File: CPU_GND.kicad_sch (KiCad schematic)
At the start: 1 part

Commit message: Added LGA1151 socket bracket holes
stolen from another lga1151 footprint that has wrong pin numbers....
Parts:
- JCPU1: footprint A-my-stuff:LGA-1151_L47.1-W42.5-P0.91_PE115127-4041-01H -> A-my-stuff:LGA1151_TE-2287402-1
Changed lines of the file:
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@@
 			)
 		)
-		(property "Footprint" "A-my-stuff:LGA-1151_L47.1-W42.5-P0.91_PE115127-4041-01H"
+		(property "Footprint" "A-my-stuff:LGA1151_TE-2287402-1"
 			(at 203.2 256.54 0)
 			(effects
@@
 			)
 		)
-		(property "Footprint" "A-my-stuff:LGA-1151_L47.1-W42.5-P0.91_PE115127-4041-01H"
+		(property "Footprint" "A-my-stuff:LGA1151_TE-2287402-1"
 			(at 76.2 256.54 0)
 			(effects
@@
 			)
 		)
-		(property "Footprint" "A-my-stuff:LGA-1151_L47.1-W42.5-P0.91_PE115127-4041-01H"
+		(property "Footprint" "A-my-stuff:LGA1151_TE-2287402-1"
 			(at 139.7 256.54 0)
 			(effects

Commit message: Added CPU CFG resistors
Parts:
- JCPU1: footprint A-my-stuff:LGA1151_TE-2287402-1 -> A-my-stuff:LGA-1151_L47.1-W42.5-P0.91_PE115127-4041-01H
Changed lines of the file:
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@@
 			)
 		)
-		(property "Footprint" "A-my-stuff:LGA1151_TE-2287402-1"
+		(property "Footprint" "A-my-stuff:LGA-1151_L47.1-W42.5-P0.91_PE115127-4041-01H"
 			(at 203.2 256.54 0)
 			(effects
@@
 			)
 		)
-		(property "Footprint" "A-my-stuff:LGA1151_TE-2287402-1"
+		(property "Footprint" "A-my-stuff:LGA-1151_L47.1-W42.5-P0.91_PE115127-4041-01H"
 			(at 76.2 256.54 0)
 			(effects
@@
 			)
 		)
-		(property "Footprint" "A-my-stuff:LGA1151_TE-2287402-1"
+		(property "Footprint" "A-my-stuff:LGA-1151_L47.1-W42.5-P0.91_PE115127-4041-01H"
 			(at 139.7 256.54 0)
 			(effects

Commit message: stroopwafel.exe
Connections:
- net GND: no longer JCPU1.A11 (VSS), JCPU1.A13 (VSS), JCPU1.A15 (VSS), JCPU1.A17 (VSS), JCPU1.A24 (VSS), JCPU1.A4 (VSS), JCPU1.A7 (VSS), JCPU1.AA3 (VSS), JCPU1.AA33 (VSS), JCPU1.AA8 (VSS), JCPU1.AB39 (VSS), JCPU1.AB5 (VSS), JCPU1.AC3 (VSS), JCPU1.AC33 (VSS), JCPU1.AC34 (VSS), JCPU1.AC35 (VSS), JCPU1.AC6 (VSS), JCPU1.AD1 (VSS), JCPU1.AD33 (VSS), JCPU1.AD36 (VSS), JCPU1.AD37 (VSS), JCPU1.AD38 (VSS), JCPU1.AD39 (VSS), JCPU1.AD4 (VSS), JCPU1.AD40 (VSS), JCPU1.AD6 (VSS), JCPU1.AD7 (VSS), JCPU1.AD8 (VSS), JCPU1.AE3 (VSS), JCPU1.AE33 (VSS), JCPU1.AE36 (VSS), JCPU1.AE5 (VSS), JCPU1.AE8 (VSS), JCPU1.AF1 (VSS), JCPU1.AF33 (VSS), JCPU1.AF36 (VSS), JCPU1.AF37 (VSS), JCPU1.AF40 (VSS), JCPU1.AF5 (VSS), JCPU1.AF8 (VSS), JCPU1.AG1 (VSS), JCPU1.AG2 (VSS), JCPU1.AG3 (VSS), JCPU1.AG33 (VSS), JCPU1.AG36 (VSS), JCPU1.AG4 (VSS), JCPU1.AG5 (VSS), JCPU1.AG8 (VSS), JCPU1.AH33 (VSS), JCPU1.AH36 (VSS), JCPU1.AH37 (VSS), JCPU1.AH38 (VSS), JCPU1.AH39 (VSS), JCPU1.AH40 (VSS), JCPU1.AH5 (VSS), JCPU1.AH8 (VSS), JCPU1.AJ1 (VSS), JCPU1.AJ24 (VSS), JCPU1.AJ30 (VSS), JCPU1.AJ31 (VSS), JCPU1.AJ32 (VSS), JCPU1.AJ33 (VSS), JCPU1.AJ34 (VSS), JCPU1.AJ35 (VSS), JCPU1.AJ36 (VSS), JCPU1.AJ4 (VSS), JCPU1.AJ5 (VSS), JCPU1.AJ8 (VSS), JCPU1.AK10 (VSS), JCPU1.AK12 (VSS), JCPU1.AK13 (VSS), JCPU1.AK15 (VSS), JCPU1.AK16 (VSS), JCPU1.AK17 (VSS), JCPU1.AK18 (VSS), JCPU1.AK19 (VSS), JCPU1.AK20 (VSS), JCPU1.AK22 (VSS), JCPU1.AK23 (VSS), JCPU1.AK25 (VSS), JCPU1.AK26 (VSS), JCPU1.AK27 (VSS), JCPU1.AK28 (VSS), JCPU1.AK29 (VSS), JCPU1.AK30 (VSS), JCPU1.AK36 (VSS), JCPU1.AK37 (VSS), JCPU1.AK40 (VSS), JCPU1.AK5 (VSS), JCPU1.AK6 (VSS), JCPU1.AK7 (VSS), JCPU1.AK8 (VSS), JCPU1.AK9 (VSS), JCPU1.AL1 (VSS), JCPU1.AL11 (VSS), JCPU1.AL14 (VSS), JCPU1.AL2 (VSS), JCPU1.AL21 (VSS), JCPU1.AL24 (VSS), JCPU1.AL27 (VSS), JCPU1.AL3 (VSS), JCPU1.AL30 (VSS), JCPU1.AL36 (VSS), JCPU1.AL4 (VSS), JCPU1.AL5 (VSS), JCPU1.AM11 (VSS), JCPU1.AM14 (VSS), JCPU1.AM17 (VSS), JCPU1.AM19 (VSS), JCPU1.AM24 (VSS), JCPU1.AM27 (VSS), JCPU1.AM30 (VSS), JCPU1.AM31 (VSS), JCPU1.AM32 (VSS), JCPU1.AM33 (VSS), JCPU1.AM34 (VSS), JCPU1.AM35 (VSS), JCPU1.AM36 (VSS), JCPU1.AM37 (VSS), JCPU1.AM38 (VSS), JCPU1.AM39 (VSS), JCPU1.AM40 (VSS), JCPU1.AM5 (VSS), JCPU1.AN1 (VSS), JCPU1.AN10 (VSS), JCPU1.AN11 (VSS), JCPU1.AN14 (VSS), JCPU1.AN16 (VSS), JCPU1.AN19 (VSS), JCPU1.AN22 (VSS), JCPU1.AN23 (VSS), JCPU1.AN24 (VSS), JCPU1.AN27 (VSS), JCPU1.AN30 (VSS), JCPU1.AN36 (VSS), JCPU1.AN4 (VSS), JCPU1.AN5 (VSS), JCPU1.AN6 (VSS), JCPU1.AN7 (VSS), JCPU1.AN8 (VSS), JCPU1.AN9 (VSS), JCPU1.AP11 (VSS), JCPU1.AP14 (VSS), JCPU1.AP24 (VSS), JCPU1.AP27 (VSS), JCPU1.AP30 (VSS), JCPU1.AP36 (VSS), JCPU1.AP37 (VSS), JCPU1.AP40 (VSS), JCPU1.AP5 (VSS), JCPU1.AR1 (VSS), JCPU1.AR11 (VSS), JCPU1.AR14 (VSS), JCPU1.AR16 (VSS), JCPU1.AR17 (VSS), JCPU1.AR18 (VSS), JCPU1.AR19 (VSS), JCPU1.AR2 (VSS), JCPU1.AR20 (VSS), JCPU1.AR21 (VSS), JCPU1.AR22 (VSS), JCPU1.AR23 (VSS), JCPU1.AR24 (VSS), JCPU1.AR27 (VSS), JCPU1.AR3 (VSS), JCPU1.AR30 (VSS), JCPU1.AR31 (VSS), JCPU1.AR32 (VSS), JCPU1.AR33 (VSS), JCPU1.AR34 (VSS), JCPU1.AR35 (VSS), JCPU1.AR36 (VSS), JCPU1.AR4 (VSS), JCPU1.AR5 (VSS), JCPU1.AT10 (VSS), JCPU1.AT11 (VSS), JCPU1.AT12 (VSS), JCPU1.AT13 (VSS), JCPU1.AT14 (VSS), JCPU1.AT15 (VSS), JCPU1.AT17 (VSS), JCPU1.AT24 (VSS), JCPU1.AT25 (VSS), JCPU1.AT26 (VSS), JCPU1.AT27 (VSS), JCPU1.AT28 (VSS), JCPU1.AT29 (VSS), JCPU1.AT30 (VSS), JCPU1.AT31 (VSS), JCPU1.AT32 (VSS), JCPU1.AT34 (VSS), JCPU1.AT36 (VSS), JCPU1.AT37 (VSS), JCPU1.AT38 (VSS), JCPU1.AT39 (VSS), JCPU1.AT40 (VSS), JCPU1.AT5 (VSS), JCPU1.AT6 (VSS), JCPU1.AT7 (VSS), JCPU1.AT8 (VSS), JCPU1.AT9 (VSS), JCPU1.AU1 (VSS), JCPU1.AU25 (VSS), JCPU1.AU30 (VSS), JCPU1.AU34 (VSS), JCPU1.AU39 (VSS), JCPU1.AU4 (VSS), JCPU1.AU40 (VSS), JCPU1.AU5 (VSS), JCPU1.AU7 (VSS), JCPU1.AV2 (VSS), JCPU1.AV26 (VSS), JCPU1.AV28 (VSS), JCPU1.AV30 (VSS), JCPU1.AV34 (VSS), JCPU1.AV38 (VSS), JCPU1.AV39 (VSS), JCPU1.AV5 (VSS), JCPU1.AV9 (VSS), JCPU1.AW3 (VSS), JCPU1.AW30 (VSS), JCPU1.AW32 (VSS), JCPU1.AW34 (VSS), JCPU1.AW36 (VSS), JCPU1.AW38 (VSS), JCPU1.AW5 (VSS), JCPU1.AW9 (VSS), JCPU1.AY27 (VSS), JCPU1.AY30 (VSS), JCPU1.AY5 (VSS), JCPU1.AY7 (VSS), JCPU1.AY9 (VSS), JCPU1.B24 (VSS), JCPU1.B26 (VSS), JCPU1.B28 (VSS), JCPU1.B30 (VSS), JCPU1.B38 (VSS), JCPU1.B6 (VSS), JCPU1.C10 (VSS), JCPU1.C12 (VSS), JCPU1.C14 (VSS), JCPU1.C16 (VSS), JCPU1.C18 (VSS), JCPU1.C2 (VSS), JCPU1.C20 (VSS), JCPU1.C22 (VSS), JCPU1.C24 (VSS), JCPU1.C31 (VSS), JCPU1.C33 (VSS), JCPU1.C35 (VSS), JCPU1.C37 (VSS), JCPU1.C5 (VSS), JCPU1.C8 (VSS), JCPU1.D24 (VSS), JCPU1.D26 (VSS), JCPU1.D28 (VSS), JCPU1.D30 (VSS), JCPU1.D37 (VSS), JCPU1.D39 (VSS), JCPU1.D4 (VSS), JCPU1.D40 (VSS), JCPU1.D7 (VSS), JCPU1.E11 (VSS), JCPU1.E13 (VSS), JCPU1.E15 (VSS), JCPU1.E17 (VSS), JCPU1.E19 (VSS), JCPU1.E21 (VSS), JCPU1.E23 (VSS), JCPU1.E3 (VSS), JCPU1.E31 (VSS), JCPU1.E33 (VSS), JCPU1.E35 (VSS), JCPU1.E37 (VSS), JCPU1.E6 (VSS), JCPU1.E9 (VSS), JCPU1.F1 (VSS), JCPU1.F10 (VSS), JCPU1.F22 (VSS), JCPU1.F26 (VSS), JCPU1.F28 (VSS), JCPU1.F30 (VSS), JCPU1.F36 (VSS), JCPU1.F4 (VSS), JCPU1.F40 (VSS), JCPU1.F7 (VSS), JCPU1.G11 (VSS), JCPU1.G13 (VSS), JCPU1.G15 (VSS), JCPU1.G17 (VSS), JCPU1.G19 (VSS), JCPU1.G22 (VSS), JCPU1.G3 (VSS), JCPU1.G31 (VSS), JCPU1.G33 (VSS), JCPU1.G6 (VSS), JCPU1.H1 (VSS), JCPU1.H11 (VSS), JCPU1.H12 (VSS), JCPU1.H21 (VSS), JCPU1.H24 (VSS), JCPU1.H26 (VSS), JCPU1.H28 (VSS), JCPU1.H30 (VSS), JCPU1.H35 (VSS), JCPU1.H37 (VSS), JCPU1.H39 (VSS), JCPU1.H4 (VSS), JCPU1.H7 (VSS), JCPU1.H9 (VSS), JCPU1.J10 (VSS), JCPU1.J12 (VSS), JCPU1.J16 (VSS), JCPU1.J18 (VSS), JCPU1.J20 (VSS), JCPU1.J3 (VSS), JCPU1.J32 (VSS), JCPU1.J34 (VSS), JCPU1.J6 (VSS), JCPU1.K1 (VSS), JCPU1.K14 (VSS), JCPU1.K15 (VSS), JCPU1.K17 (VSS), JCPU1.K19 (VSS), JCPU1.K22 (VSS), JCPU1.K24 (VSS), JCPU1.K26 (VSS), JCPU1.K28 (VSS), JCPU1.K30 (VSS), JCPU1.K33 (VSS), JCPU1.K35 (VSS), JCPU1.K37 (VSS), JCPU1.K39 (VSS), JCPU1.K4 (VSS), JCPU1.K7 (VSS), JCPU1.L11 (VSS), JCPU1.L13 (VSS), JCPU1.L3 (VSS), JCPU1.L32 (VSS), JCPU1.L6 (VSS), JCPU1.L9 (VSS), JCPU1.M1 (VSS), JCPU1.M10 (VSS), JCPU1.M12 (VSS), JCPU1.M15 (VSS), JCPU1.M17 (VSS), JCPU1.M19 (VSS), JCPU1.M21 (VSS), JCPU1.M23 (VSS), JCPU1.M25 (VSS), JCPU1.M27 (VSS), JCPU1.M29 (VSS), JCPU1.M35 (VSS), JCPU1.M37 (VSS), JCPU1.M39 (VSS), JCPU1.M4 (VSS), JCPU1.M7 (VSS), JCPU1.N3 (VSS), JCPU1.N33 (VSS), JCPU1.N6 (VSS), JCPU1.N8 (VSS), JCPU1.P1 (VSS), JCPU1.P35 (VSS), JCPU1.P37 (VSS), JCPU1.P39 (VSS), JCPU1.P4 (VSS), JCPU1.R3 (VSS), JCPU1.R33 (VSS), JCPU1.R6 (VSS), JCPU1.R8 (VSS), JCPU1.T1 (VSS), JCPU1.T35 (VSS), JCPU1.T37 (VSS), JCPU1.T39 (VSS), JCPU1.T4 (VSS), JCPU1.U3 (VSS), JCPU1.U33 (VSS), JCPU1.U6 (VSS), JCPU1.V1 (VSS), JCPU1.V35 (VSS), JCPU1.V37 (VSS), JCPU1.V39 (VSS), JCPU1.V8 (VSS), JCPU1.W3 (VSS), JCPU1.W33 (VSS), JCPU1.W6 (VSS), JCPU1.Y35 (VSS), JCPU1.Y37 (VSS), JCPU1.Y5 (VSS)
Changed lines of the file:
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@@
 		(pin "1"
 		)
-		(instances
-			(project ""
-				(path "/4bc771b8-eb19-46d0-8798-27231a7c6e83/61df14ea-2065-4751-84ed-7e7cf71220e9"
-					(reference "#PWR1")
-					(unit 1)
-				)
-			)
-		)
 	)
 	(symbol
@@
 		(lib_id "A-my-stuff:Intel_CFL_1151")
 		(at 203.2 144.78 0)
-		(unit 12)
+		(unit 1)
 		(exclude_from_sim no)
 		(in_bom yes)
@@
 		(pin "J5"
 		)
-		(instances
-			(project ""
-				(path "/4bc771b8-eb19-46d0-8798-27231a7c6e83/061fe2d6-87c2-48c2-90bb-0928700512fc"
-					(reference "JCPU1")
-					(unit 12)
-				)
-				(path "/4bc771b8-eb19-46d0-8798-27231a7c6e83/61df14ea-2065-4751-84ed-7e7cf71220e9"
-					(reference "JCPU1")
-					(unit 12)
-				)
-			)
-		)
 	)
 	(symbol
@@
 		(lib_id "A-my-stuff:Intel_CFL_1151")
 		(at 76.2 144.78 0)
-		(unit 6)
+		(unit 1)
 		(exclude_from_sim no)
 		(in_bom yes)
@@
 		(pin "J5"
 		)
-		(instances
-			(project ""
-				(path "/4bc771b8-eb19-46d0-8798-27231a7c6e83/061fe2d6-87c2-48c2-90bb-0928700512fc"
-					(reference "JCPU1")
-					(unit 6)
-				)
-				(path "/4bc771b8-eb19-46d0-8798-27231a7c6e83/61df14ea-2065-4751-84ed-7e7cf71220e9"
-					(reference "JCPU1")
-					(unit 6)
-				)
-			)
-		)
 	)
 	(symbol
@@
 		(lib_id "A-my-stuff:Intel_CFL_1151")
 		(at 139.7 144.78 0)
-		(unit 11)
+		(unit 1)
 		(exclude_from_sim no)
 		(in_bom yes)
@@
 		(pin "J5"
 		)
-		(instances
-			(project ""
-				(path "/4bc771b8-eb19-46d0-8798-27231a7c6e83/061fe2d6-87c2-48c2-90bb-0928700512fc"
-					(reference "JCPU1")
-					(unit 11)
-				)
-				(path "/4bc771b8-eb19-46d0-8798-27231a7c6e83/61df14ea-2065-4751-84ed-7e7cf71220e9"
-					(reference "JCPU1")
-					(unit 11)
-				)
-			)
-		)
 	)

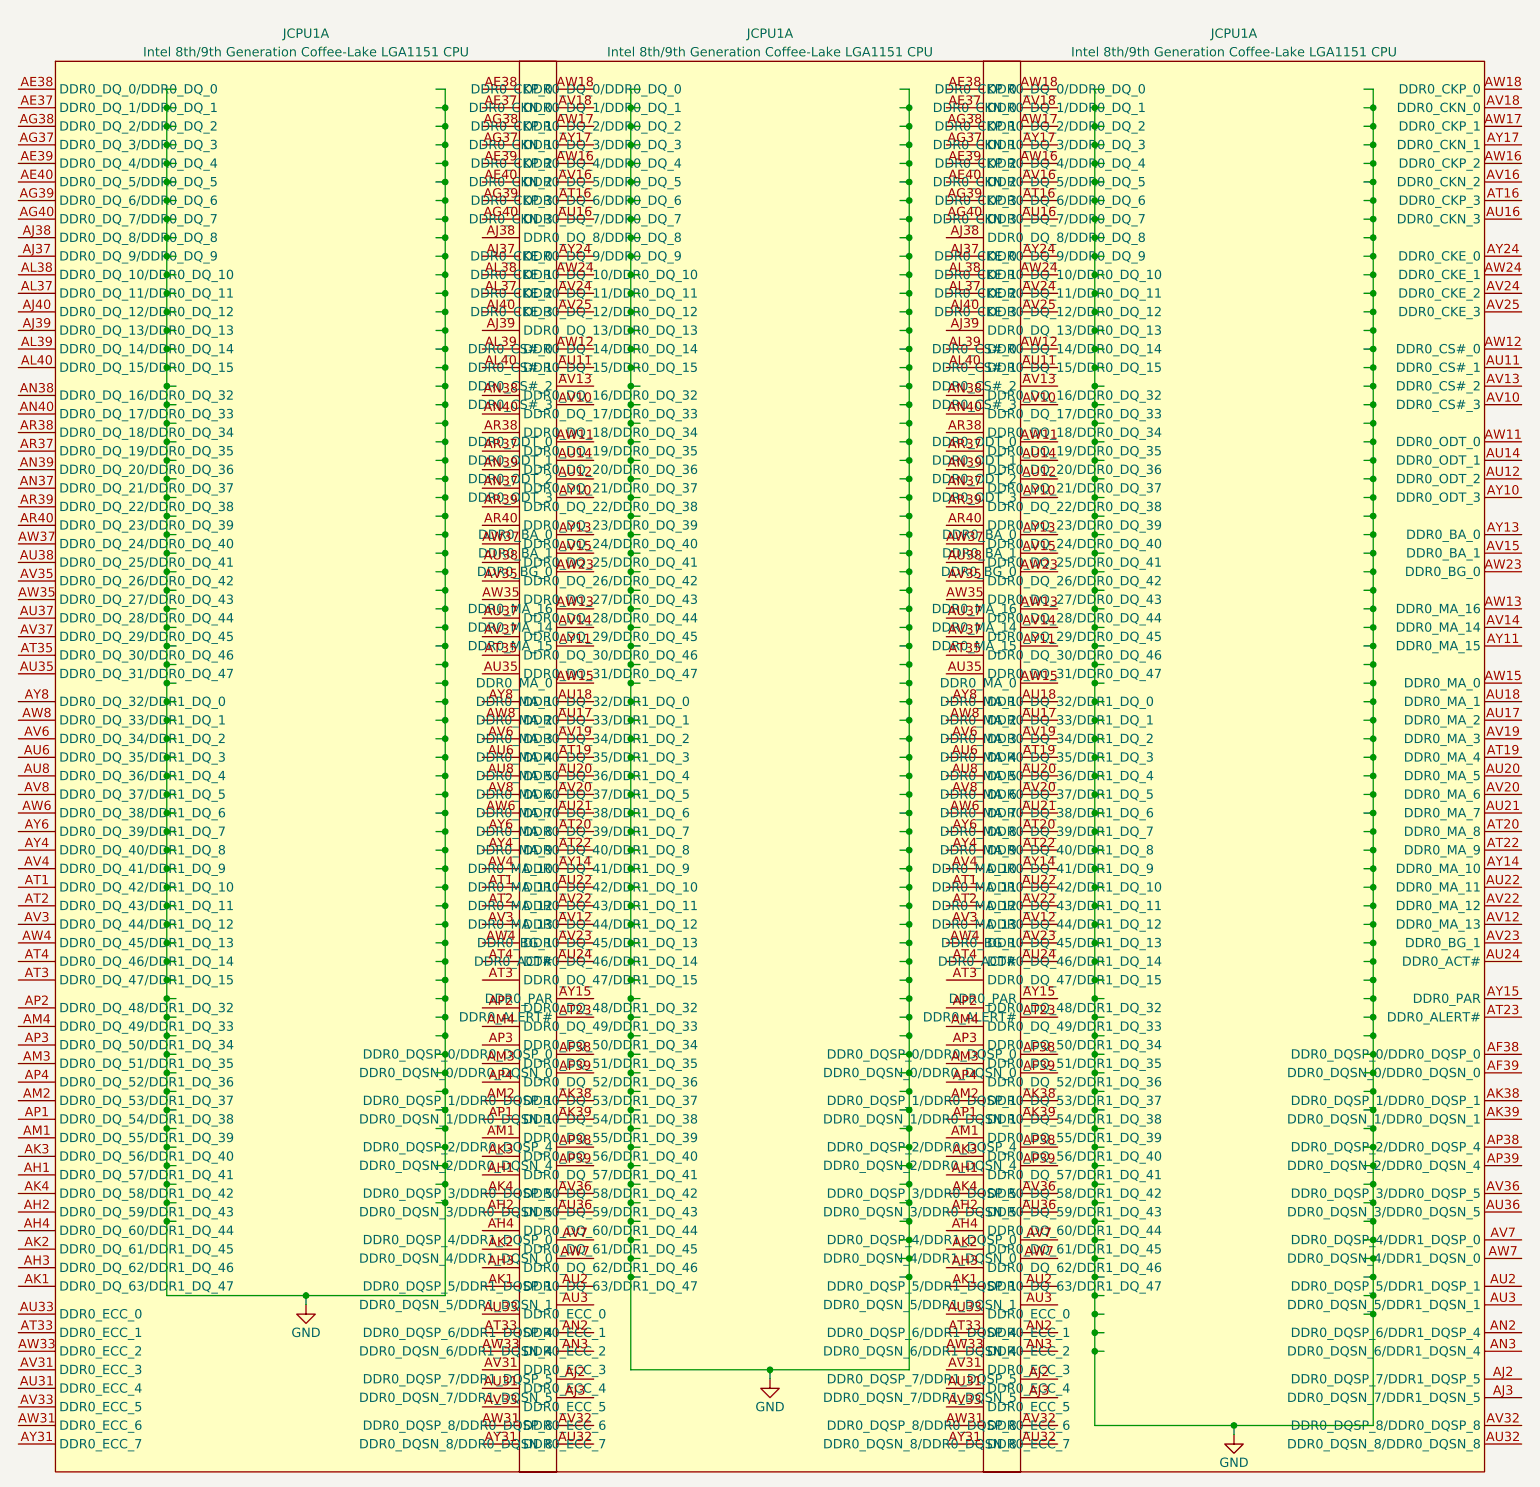
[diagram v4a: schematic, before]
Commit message: Fixed entire schematic being broken
somehow every symbol with index 1 broke and updating the pcb stopped working. how does that even happen. oh well it's fixed now
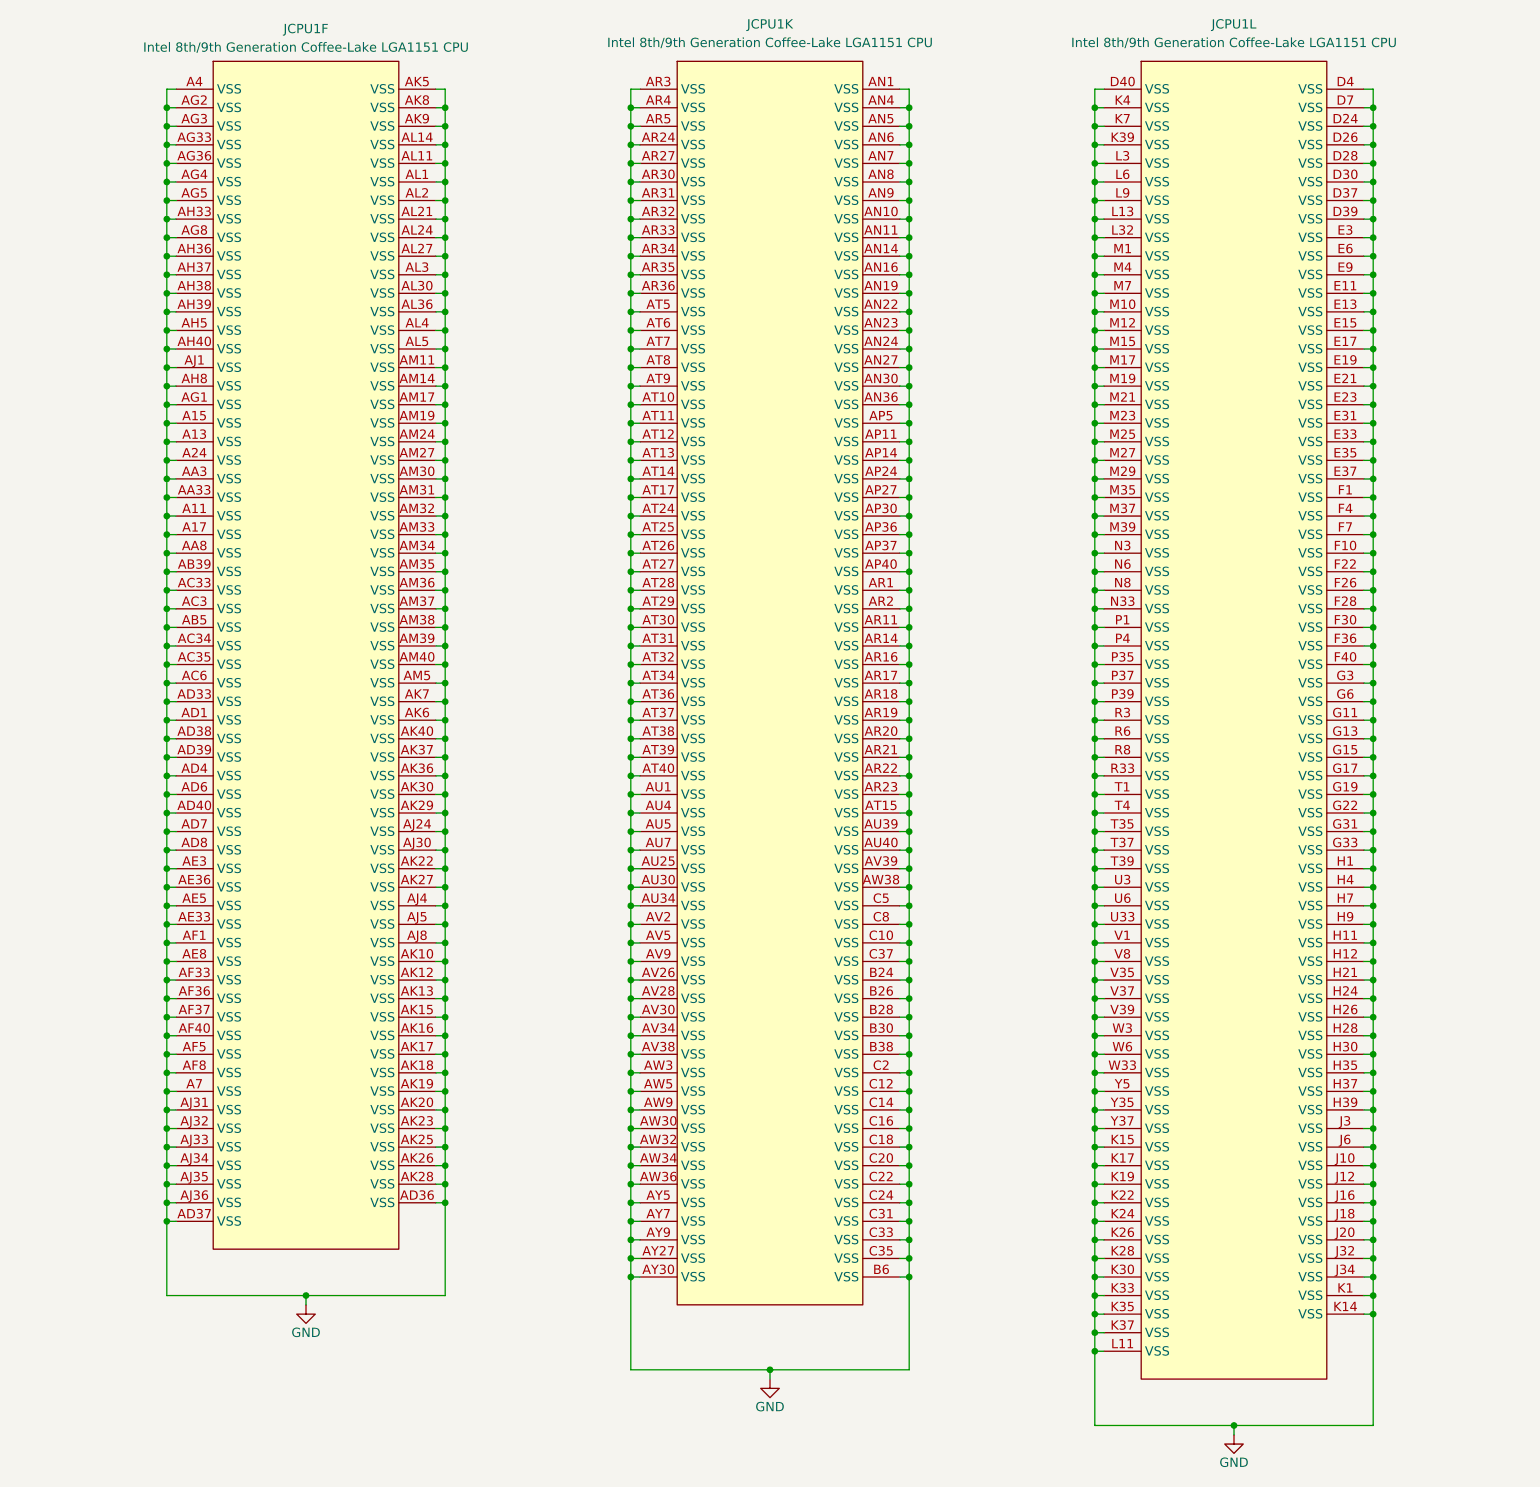
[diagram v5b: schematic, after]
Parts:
- removed JCPU1 (x3): Intel 8th/9th Generation Coffee-Lake LGA1151 CPU, A-my-stuff:LGA-1151_L47.1-W42.5-P0.91_PE115127-4041-01H, symbol A-my-stuff:Intel_CFL_1151
- added JCPU1: Intel 8th/9th Generation Coffee-Lake LGA1151 CPU, A-my-stuff:LGA-1151_L47.1-W42.5-P0.91_PE115127-4041-01H, symbol A-my-stuff:Intel_CFL_1151
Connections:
- net GND: now also JCPU1.A11 (VSS), JCPU1.A13 (VSS), JCPU1.A15 (VSS), JCPU1.A17 (VSS), JCPU1.A24 (VSS), JCPU1.A4 (VSS), JCPU1.A7 (VSS), JCPU1.AA3 (VSS), JCPU1.AA33 (VSS), JCPU1.AA8 (VSS), JCPU1.AB39 (VSS), JCPU1.AB5 (VSS), JCPU1.AC3 (VSS), JCPU1.AC33 (VSS), JCPU1.AC34 (VSS), JCPU1.AC35 (VSS), JCPU1.AC6 (VSS), JCPU1.AD1 (VSS), JCPU1.AD33 (VSS), JCPU1.AD36 (VSS), JCPU1.AD37 (VSS), JCPU1.AD38 (VSS), JCPU1.AD39 (VSS), JCPU1.AD4 (VSS), JCPU1.AD40 (VSS), JCPU1.AD6 (VSS), JCPU1.AD7 (VSS), JCPU1.AD8 (VSS), JCPU1.AE3 (VSS), JCPU1.AE33 (VSS), JCPU1.AE36 (VSS), JCPU1.AE5 (VSS), JCPU1.AE8 (VSS), JCPU1.AF1 (VSS), JCPU1.AF33 (VSS), JCPU1.AF36 (VSS), JCPU1.AF37 (VSS), JCPU1.AF40 (VSS), JCPU1.AF5 (VSS), JCPU1.AF8 (VSS), JCPU1.AG1 (VSS), JCPU1.AG2 (VSS), JCPU1.AG3 (VSS), JCPU1.AG33 (VSS), JCPU1.AG36 (VSS), JCPU1.AG4 (VSS), JCPU1.AG5 (VSS), JCPU1.AG8 (VSS), JCPU1.AH33 (VSS), JCPU1.AH36 (VSS), JCPU1.AH37 (VSS), JCPU1.AH38 (VSS), JCPU1.AH39 (VSS), JCPU1.AH40 (VSS), JCPU1.AH5 (VSS), JCPU1.AH8 (VSS), JCPU1.AJ1 (VSS), JCPU1.AJ24 (VSS), JCPU1.AJ30 (VSS), JCPU1.AJ31 (VSS), JCPU1.AJ32 (VSS), JCPU1.AJ33 (VSS), JCPU1.AJ34 (VSS), JCPU1.AJ35 (VSS), JCPU1.AJ36 (VSS), JCPU1.AJ4 (VSS), JCPU1.AJ5 (VSS), JCPU1.AJ8 (VSS), JCPU1.AK10 (VSS), JCPU1.AK12 (VSS), JCPU1.AK13 (VSS), JCPU1.AK15 (VSS), JCPU1.AK16 (VSS), JCPU1.AK17 (VSS), JCPU1.AK18 (VSS), JCPU1.AK19 (VSS), JCPU1.AK20 (VSS), JCPU1.AK22 (VSS), JCPU1.AK23 (VSS), JCPU1.AK25 (VSS), JCPU1.AK26 (VSS), JCPU1.AK27 (VSS), JCPU1.AK28 (VSS), JCPU1.AK29 (VSS), JCPU1.AK30 (VSS), JCPU1.AK36 (VSS), JCPU1.AK37 (VSS), JCPU1.AK40 (VSS), JCPU1.AK5 (VSS), JCPU1.AK6 (VSS), JCPU1.AK7 (VSS), JCPU1.AK8 (VSS), JCPU1.AK9 (VSS), JCPU1.AL1 (VSS), JCPU1.AL11 (VSS), JCPU1.AL14 (VSS), JCPU1.AL2 (VSS), JCPU1.AL21 (VSS), JCPU1.AL24 (VSS), JCPU1.AL27 (VSS), JCPU1.AL3 (VSS), JCPU1.AL30 (VSS), JCPU1.AL36 (VSS), JCPU1.AL4 (VSS), JCPU1.AL5 (VSS), JCPU1.AM11 (VSS), JCPU1.AM14 (VSS), JCPU1.AM17 (VSS), JCPU1.AM19 (VSS), JCPU1.AM24 (VSS), JCPU1.AM27 (VSS), JCPU1.AM30 (VSS), JCPU1.AM31 (VSS), JCPU1.AM32 (VSS), JCPU1.AM33 (VSS), JCPU1.AM34 (VSS), JCPU1.AM35 (VSS), JCPU1.AM36 (VSS), JCPU1.AM37 (VSS), JCPU1.AM38 (VSS), JCPU1.AM39 (VSS), JCPU1.AM40 (VSS), JCPU1.AM5 (VSS), JCPU1.AN1 (VSS), JCPU1.AN10 (VSS), JCPU1.AN11 (VSS), JCPU1.AN14 (VSS), JCPU1.AN16 (VSS), JCPU1.AN19 (VSS), JCPU1.AN22 (VSS), JCPU1.AN23 (VSS), JCPU1.AN24 (VSS), JCPU1.AN27 (VSS), JCPU1.AN30 (VSS), JCPU1.AN36 (VSS), JCPU1.AN4 (VSS), JCPU1.AN5 (VSS), JCPU1.AN6 (VSS), JCPU1.AN7 (VSS), JCPU1.AN8 (VSS), JCPU1.AN9 (VSS), JCPU1.AP11 (VSS), JCPU1.AP14 (VSS), JCPU1.AP24 (VSS), JCPU1.AP27 (VSS), JCPU1.AP30 (VSS), JCPU1.AP36 (VSS), JCPU1.AP37 (VSS), JCPU1.AP40 (VSS), JCPU1.AP5 (VSS), JCPU1.AR1 (VSS), JCPU1.AR11 (VSS), JCPU1.AR14 (VSS), JCPU1.AR16 (VSS), JCPU1.AR17 (VSS), JCPU1.AR18 (VSS), JCPU1.AR19 (VSS), JCPU1.AR2 (VSS), JCPU1.AR20 (VSS), JCPU1.AR21 (VSS), JCPU1.AR22 (VSS), JCPU1.AR23 (VSS), JCPU1.AR24 (VSS), JCPU1.AR27 (VSS), JCPU1.AR3 (VSS), JCPU1.AR30 (VSS), JCPU1.AR31 (VSS), JCPU1.AR32 (VSS), JCPU1.AR33 (VSS), JCPU1.AR34 (VSS), JCPU1.AR35 (VSS), JCPU1.AR36 (VSS), JCPU1.AR4 (VSS), JCPU1.AR5 (VSS), JCPU1.AT10 (VSS), JCPU1.AT11 (VSS), JCPU1.AT12 (VSS), JCPU1.AT13 (VSS), JCPU1.AT14 (VSS), JCPU1.AT15 (VSS), JCPU1.AT17 (VSS), JCPU1.AT24 (VSS), JCPU1.AT25 (VSS), JCPU1.AT26 (VSS), JCPU1.AT27 (VSS), JCPU1.AT28 (VSS), JCPU1.AT29 (VSS), JCPU1.AT30 (VSS), JCPU1.AT31 (VSS), JCPU1.AT32 (VSS), JCPU1.AT34 (VSS), JCPU1.AT36 (VSS), JCPU1.AT37 (VSS), JCPU1.AT38 (VSS), JCPU1.AT39 (VSS), JCPU1.AT40 (VSS), JCPU1.AT5 (VSS), JCPU1.AT6 (VSS), JCPU1.AT7 (VSS), JCPU1.AT8 (VSS), JCPU1.AT9 (VSS), JCPU1.AU1 (VSS), JCPU1.AU25 (VSS), JCPU1.AU30 (VSS), JCPU1.AU34 (VSS), JCPU1.AU39 (VSS), JCPU1.AU4 (VSS), JCPU1.AU40 (VSS), JCPU1.AU5 (VSS), JCPU1.AU7 (VSS), JCPU1.AV2 (VSS), JCPU1.AV26 (VSS), JCPU1.AV28 (VSS), JCPU1.AV30 (VSS), JCPU1.AV34 (VSS), JCPU1.AV38 (VSS), JCPU1.AV39 (VSS), JCPU1.AV5 (VSS), JCPU1.AV9 (VSS), JCPU1.AW3 (VSS), JCPU1.AW30 (VSS), JCPU1.AW32 (VSS), JCPU1.AW34 (VSS), JCPU1.AW36 (VSS), JCPU1.AW38 (VSS), JCPU1.AW5 (VSS), JCPU1.AW9 (VSS), JCPU1.AY27 (VSS), JCPU1.AY30 (VSS), JCPU1.AY5 (VSS), JCPU1.AY7 (VSS), JCPU1.AY9 (VSS), JCPU1.B24 (VSS), JCPU1.B26 (VSS), JCPU1.B28 (VSS), JCPU1.B30 (VSS), JCPU1.B38 (VSS), JCPU1.B6 (VSS), JCPU1.C10 (VSS), JCPU1.C12 (VSS), JCPU1.C14 (VSS), JCPU1.C16 (VSS), JCPU1.C18 (VSS), JCPU1.C2 (VSS), JCPU1.C20 (VSS), JCPU1.C22 (VSS), JCPU1.C24 (VSS), JCPU1.C31 (VSS), JCPU1.C33 (VSS), JCPU1.C35 (VSS), JCPU1.C37 (VSS), JCPU1.C5 (VSS), JCPU1.C8 (VSS), JCPU1.D24 (VSS), JCPU1.D26 (VSS), JCPU1.D28 (VSS), JCPU1.D30 (VSS), JCPU1.D37 (VSS), JCPU1.D39 (VSS), JCPU1.D4 (VSS), JCPU1.D40 (VSS), JCPU1.D7 (VSS), JCPU1.E11 (VSS), JCPU1.E13 (VSS), JCPU1.E15 (VSS), JCPU1.E17 (VSS), JCPU1.E19 (VSS), JCPU1.E21 (VSS), JCPU1.E23 (VSS), JCPU1.E3 (VSS), JCPU1.E31 (VSS), JCPU1.E33 (VSS), JCPU1.E35 (VSS), JCPU1.E37 (VSS), JCPU1.E6 (VSS), JCPU1.E9 (VSS), JCPU1.F1 (VSS), JCPU1.F10 (VSS), JCPU1.F22 (VSS), JCPU1.F26 (VSS), JCPU1.F28 (VSS), JCPU1.F30 (VSS), JCPU1.F36 (VSS), JCPU1.F4 (VSS), JCPU1.F40 (VSS), JCPU1.F7 (VSS), JCPU1.G11 (VSS), JCPU1.G13 (VSS), JCPU1.G15 (VSS), JCPU1.G17 (VSS), JCPU1.G19 (VSS), JCPU1.G22 (VSS), JCPU1.G3 (VSS), JCPU1.G31 (VSS), JCPU1.G33 (VSS), JCPU1.G6 (VSS), JCPU1.H1 (VSS), JCPU1.H11 (VSS), JCPU1.H12 (VSS), JCPU1.H21 (VSS), JCPU1.H24 (VSS), JCPU1.H26 (VSS), JCPU1.H28 (VSS), JCPU1.H30 (VSS), JCPU1.H35 (VSS), JCPU1.H37 (VSS), JCPU1.H39 (VSS), JCPU1.H4 (VSS), JCPU1.H7 (VSS), JCPU1.H9 (VSS), JCPU1.J10 (VSS), JCPU1.J12 (VSS), JCPU1.J16 (VSS), JCPU1.J18 (VSS), JCPU1.J20 (VSS), JCPU1.J3 (VSS), JCPU1.J32 (VSS), JCPU1.J34 (VSS), JCPU1.J6 (VSS), JCPU1.K1 (VSS), JCPU1.K14 (VSS), JCPU1.K15 (VSS), JCPU1.K17 (VSS), JCPU1.K19 (VSS), JCPU1.K22 (VSS), JCPU1.K24 (VSS), JCPU1.K26 (VSS), JCPU1.K28 (VSS), JCPU1.K30 (VSS), JCPU1.K33 (VSS), JCPU1.K35 (VSS), JCPU1.K37 (VSS), JCPU1.K39 (VSS), JCPU1.K4 (VSS), JCPU1.K7 (VSS), JCPU1.L11 (VSS), JCPU1.L13 (VSS), JCPU1.L3 (VSS), JCPU1.L32 (VSS), JCPU1.L6 (VSS), JCPU1.L9 (VSS), JCPU1.M1 (VSS), JCPU1.M10 (VSS), JCPU1.M12 (VSS), JCPU1.M15 (VSS), JCPU1.M17 (VSS), JCPU1.M19 (VSS), JCPU1.M21 (VSS), JCPU1.M23 (VSS), JCPU1.M25 (VSS), JCPU1.M27 (VSS), JCPU1.M29 (VSS), JCPU1.M35 (VSS), JCPU1.M37 (VSS), JCPU1.M39 (VSS), JCPU1.M4 (VSS), JCPU1.M7 (VSS), JCPU1.N3 (VSS), JCPU1.N33 (VSS), JCPU1.N6 (VSS), JCPU1.N8 (VSS), JCPU1.P1 (VSS), JCPU1.P35 (VSS), JCPU1.P37 (VSS), JCPU1.P39 (VSS), JCPU1.P4 (VSS), JCPU1.R3 (VSS), JCPU1.R33 (VSS), JCPU1.R6 (VSS), JCPU1.R8 (VSS), JCPU1.T1 (VSS), JCPU1.T35 (VSS), JCPU1.T37 (VSS), JCPU1.T39 (VSS), JCPU1.T4 (VSS), JCPU1.U3 (VSS), JCPU1.U33 (VSS), JCPU1.U6 (VSS), JCPU1.V1 (VSS), JCPU1.V35 (VSS), JCPU1.V37 (VSS), JCPU1.V39 (VSS), JCPU1.V8 (VSS), JCPU1.W3 (VSS), JCPU1.W33 (VSS), JCPU1.W6 (VSS), JCPU1.Y35 (VSS), JCPU1.Y37 (VSS), JCPU1.Y5 (VSS)

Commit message: nooo they be stealin my stroopwafel
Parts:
- added unit 12 of JCPU1
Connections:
- net GND: now also JCPU1.D24 (VSS), JCPU1.D26 (VSS), JCPU1.D28 (VSS), JCPU1.D30 (VSS), JCPU1.D37 (VSS), JCPU1.D39 (VSS), JCPU1.D4 (VSS), JCPU1.D40 (VSS), JCPU1.D7 (VSS), JCPU1.E11 (VSS), JCPU1.E13 (VSS), JCPU1.E15 (VSS), JCPU1.E17 (VSS), JCPU1.E19 (VSS), JCPU1.E21 (VSS), JCPU1.E23 (VSS), JCPU1.E3 (VSS), JCPU1.E31 (VSS), JCPU1.E33 (VSS), JCPU1.E35 (VSS), JCPU1.E37 (VSS), JCPU1.E6 (VSS), JCPU1.E9 (VSS), JCPU1.F1 (VSS), JCPU1.F10 (VSS), JCPU1.F22 (VSS), JCPU1.F26 (VSS), JCPU1.F28 (VSS), JCPU1.F30 (VSS), JCPU1.F36 (VSS), JCPU1.F4 (VSS), JCPU1.F40 (VSS), JCPU1.F7 (VSS), JCPU1.G11 (VSS), JCPU1.G13 (VSS), JCPU1.G15 (VSS), JCPU1.G17 (VSS), JCPU1.G19 (VSS), JCPU1.G22 (VSS), JCPU1.G3 (VSS), JCPU1.G31 (VSS), JCPU1.G33 (VSS), JCPU1.G6 (VSS), JCPU1.H1 (VSS), JCPU1.H11 (VSS), JCPU1.H12 (VSS), JCPU1.H21 (VSS), JCPU1.H24 (VSS), JCPU1.H26 (VSS), JCPU1.H28 (VSS), JCPU1.H30 (VSS), JCPU1.H35 (VSS), JCPU1.H37 (VSS), JCPU1.H39 (VSS), JCPU1.H4 (VSS), JCPU1.H7 (VSS), JCPU1.H9 (VSS), JCPU1.J10 (VSS), JCPU1.J12 (VSS), JCPU1.J16 (VSS), JCPU1.J18 (VSS), JCPU1.J20 (VSS), JCPU1.J3 (VSS), JCPU1.J32 (VSS), JCPU1.J34 (VSS), JCPU1.J6 (VSS), JCPU1.K1 (VSS), JCPU1.K14 (VSS), JCPU1.K15 (VSS), JCPU1.K17 (VSS), JCPU1.K19 (VSS), JCPU1.K22 (VSS), JCPU1.K24 (VSS), JCPU1.K26 (VSS), JCPU1.K28 (VSS), JCPU1.K30 (VSS), JCPU1.K33 (VSS), JCPU1.K35 (VSS), JCPU1.K37 (VSS), JCPU1.K39 (VSS), JCPU1.K4 (VSS), JCPU1.K7 (VSS), JCPU1.L11 (VSS), JCPU1.L13 (VSS), JCPU1.L3 (VSS), JCPU1.L32 (VSS), JCPU1.L6 (VSS), JCPU1.L9 (VSS), JCPU1.M1 (VSS), JCPU1.M10 (VSS), JCPU1.M12 (VSS), JCPU1.M15 (VSS), JCPU1.M17 (VSS), JCPU1.M19 (VSS), JCPU1.M21 (VSS), JCPU1.M23 (VSS), JCPU1.M25 (VSS), JCPU1.M27 (VSS), JCPU1.M29 (VSS), JCPU1.M35 (VSS), JCPU1.M37 (VSS), JCPU1.M39 (VSS), JCPU1.M4 (VSS), JCPU1.M7 (VSS), JCPU1.N3 (VSS), JCPU1.N33 (VSS), JCPU1.N6 (VSS), JCPU1.N8 (VSS), JCPU1.P1 (VSS), JCPU1.P35 (VSS), JCPU1.P37 (VSS), JCPU1.P39 (VSS), JCPU1.P4 (VSS), JCPU1.R3 (VSS), JCPU1.R33 (VSS), JCPU1.R6 (VSS), JCPU1.R8 (VSS), JCPU1.T1 (VSS), JCPU1.T35 (VSS), JCPU1.T37 (VSS), JCPU1.T39 (VSS), JCPU1.T4 (VSS), JCPU1.U3 (VSS), JCPU1.U33 (VSS), JCPU1.U6 (VSS), JCPU1.V1 (VSS), JCPU1.V35 (VSS), JCPU1.V37 (VSS), JCPU1.V39 (VSS), JCPU1.V8 (VSS), JCPU1.W3 (VSS), JCPU1.W33 (VSS), JCPU1.W6 (VSS), JCPU1.Y35 (VSS), JCPU1.Y37 (VSS), JCPU1.Y5 (VSS); no longer JCPU1.D24 (VSS), JCPU1.D26 (VSS), JCPU1.D28 (VSS), JCPU1.D30 (VSS), JCPU1.D37 (VSS), JCPU1.D39 (VSS), JCPU1.D4 (VSS), JCPU1.D40 (VSS), JCPU1.D7 (VSS), JCPU1.E11 (VSS), JCPU1.E13 (VSS), JCPU1.E15 (VSS), JCPU1.E17 (VSS), JCPU1.E19 (VSS), JCPU1.E21 (VSS), JCPU1.E23 (VSS), JCPU1.E3 (VSS), JCPU1.E31 (VSS), JCPU1.E33 (VSS), JCPU1.E35 (VSS), JCPU1.E37 (VSS), JCPU1.E6 (VSS), JCPU1.E9 (VSS), JCPU1.F1 (VSS), JCPU1.F10 (VSS), JCPU1.F22 (VSS), JCPU1.F26 (VSS), JCPU1.F28 (VSS), JCPU1.F30 (VSS), JCPU1.F36 (VSS), JCPU1.F4 (VSS), JCPU1.F40 (VSS), JCPU1.F7 (VSS), JCPU1.G11 (VSS), JCPU1.G13 (VSS), JCPU1.G15 (VSS), JCPU1.G17 (VSS), JCPU1.G19 (VSS), JCPU1.G22 (VSS), JCPU1.G3 (VSS), JCPU1.G31 (VSS), JCPU1.G33 (VSS), JCPU1.G6 (VSS), JCPU1.H1 (VSS), JCPU1.H11 (VSS), JCPU1.H12 (VSS), JCPU1.H21 (VSS), JCPU1.H24 (VSS), JCPU1.H26 (VSS), JCPU1.H28 (VSS), JCPU1.H30 (VSS), JCPU1.H35 (VSS), JCPU1.H37 (VSS), JCPU1.H39 (VSS), JCPU1.H4 (VSS), JCPU1.H7 (VSS), JCPU1.H9 (VSS), JCPU1.J10 (VSS), JCPU1.J12 (VSS), JCPU1.J16 (VSS), JCPU1.J18 (VSS), JCPU1.J20 (VSS), JCPU1.J3 (VSS), JCPU1.J32 (VSS), JCPU1.J34 (VSS), JCPU1.J6 (VSS), JCPU1.K1 (VSS), JCPU1.K14 (VSS), JCPU1.K15 (VSS), JCPU1.K17 (VSS), JCPU1.K19 (VSS), JCPU1.K22 (VSS), JCPU1.K24 (VSS), JCPU1.K26 (VSS), JCPU1.K28 (VSS), JCPU1.K30 (VSS), JCPU1.K33 (VSS), JCPU1.K35 (VSS), JCPU1.K37 (VSS), JCPU1.K39 (VSS), JCPU1.K4 (VSS), JCPU1.K7 (VSS), JCPU1.L11 (VSS), JCPU1.L13 (VSS), JCPU1.L3 (VSS), JCPU1.L32 (VSS), JCPU1.L6 (VSS), JCPU1.L9 (VSS), JCPU1.M1 (VSS), JCPU1.M10 (VSS), JCPU1.M12 (VSS), JCPU1.M15 (VSS), JCPU1.M17 (VSS), JCPU1.M19 (VSS), JCPU1.M21 (VSS), JCPU1.M23 (VSS), JCPU1.M25 (VSS), JCPU1.M27 (VSS), JCPU1.M29 (VSS), JCPU1.M35 (VSS), JCPU1.M37 (VSS), JCPU1.M39 (VSS), JCPU1.M4 (VSS), JCPU1.M7 (VSS), JCPU1.N3 (VSS), JCPU1.N33 (VSS), JCPU1.N6 (VSS), JCPU1.N8 (VSS), JCPU1.P1 (VSS), JCPU1.P35 (VSS), JCPU1.P37 (VSS), JCPU1.P39 (VSS), JCPU1.P4 (VSS), JCPU1.R3 (VSS), JCPU1.R33 (VSS), JCPU1.R6 (VSS), JCPU1.R8 (VSS), JCPU1.T1 (VSS), JCPU1.T35 (VSS), JCPU1.T37 (VSS), JCPU1.T39 (VSS), JCPU1.T4 (VSS), JCPU1.U3 (VSS), JCPU1.U33 (VSS), JCPU1.U6 (VSS), JCPU1.V1 (VSS), JCPU1.V35 (VSS), JCPU1.V37 (VSS), JCPU1.V39 (VSS), JCPU1.V8 (VSS), JCPU1.W3 (VSS), JCPU1.W33 (VSS), JCPU1.W6 (VSS), JCPU1.Y35 (VSS), JCPU1.Y37 (VSS), JCPU1.Y5 (VSS)
